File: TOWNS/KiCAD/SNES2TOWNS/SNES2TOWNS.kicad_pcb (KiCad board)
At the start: 2 copper layers, 13 parts, among them J1 DE9_Receptacle, J2 ArduinoP2_P7, J3 ArduinoP8_P13, J4 ArduinoA5_A0, J5 ArduinoVCC_GND, J6 SNES_CONTROLLER, J7 Conn_02x03_Odd_Even, U1 74LS157, U2 74LS157

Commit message: Change of plan.  PCB version will be for Arduino NANO.
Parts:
- removed J2: ArduinoP2_P7, Connector_PinHeader_2.54mm:PinHeader_1x06_P2.54mm_Vertical
- removed J3: ArduinoP8_P13, Connector_PinHeader_2.54mm:PinHeader_1x06_P2.54mm_Vertical
- removed J4: ArduinoA5_A0, Connector_PinHeader_2.54mm:PinHeader_1x06_P2.54mm_Vertical
- removed J5: ArduinoVCC_GND, Connector_PinHeader_2.54mm:PinHeader_1x06_P2.54mm_Vertical
- added J8: ArduinoNANOP1_P15, Connector_PinSocket_2.54mm:PinSocket_1x15_P2.54mm_Vertical, F.Cu at (116.8, 104.1)
- added J9: ArduinoNANOP16_P30, Connector_PinSocket_2.54mm:PinSocket_1x15_P2.54mm_Vertical, F.Cu at (101.6, 104.1)
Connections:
- R1 pad 1: GND -> /FJ6BTN
- R1 pad 2: /CPSF -> GND
- R2 pad 1: GND -> /CPSF
- R2 pad 2: /FJ6BTN -> GND
- U1 pad 16: +5V -> unconnected-(U1-VCC-Pad16)

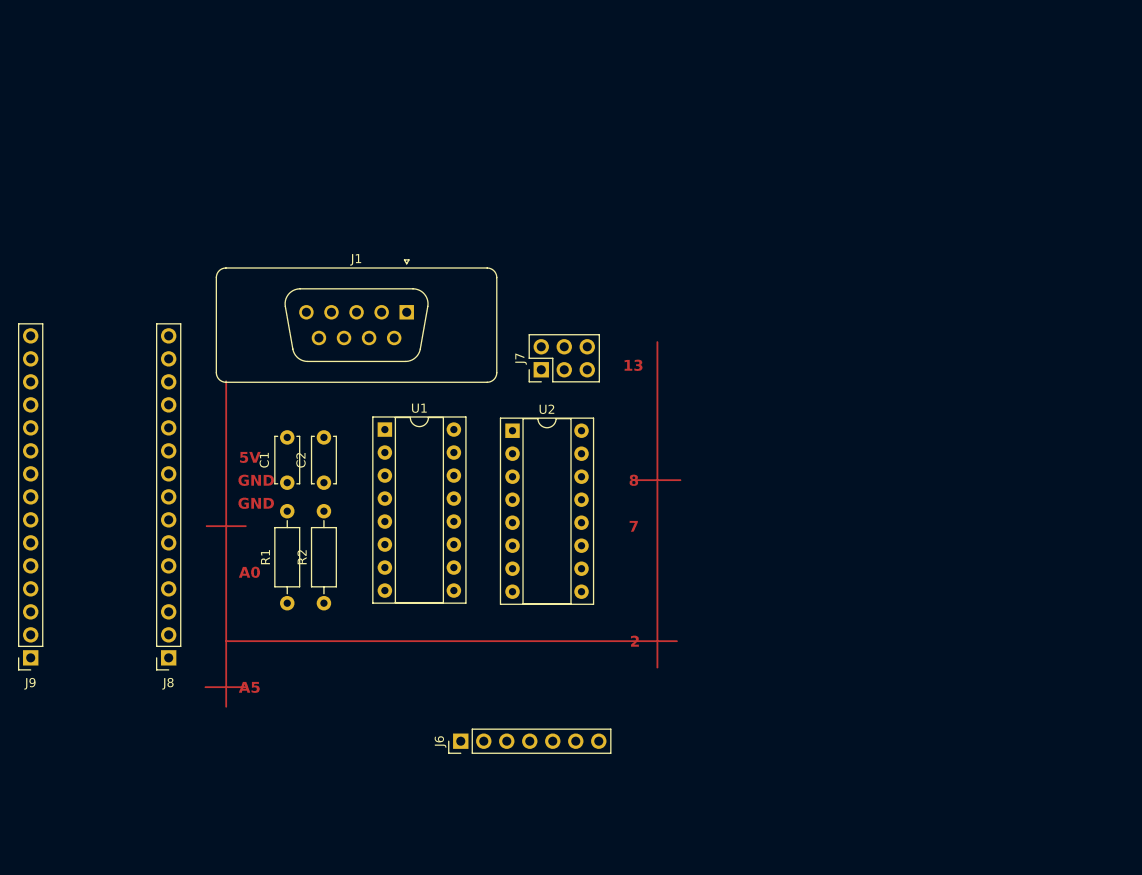
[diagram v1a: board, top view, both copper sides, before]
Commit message: PCB version will be for Arduino NANO.
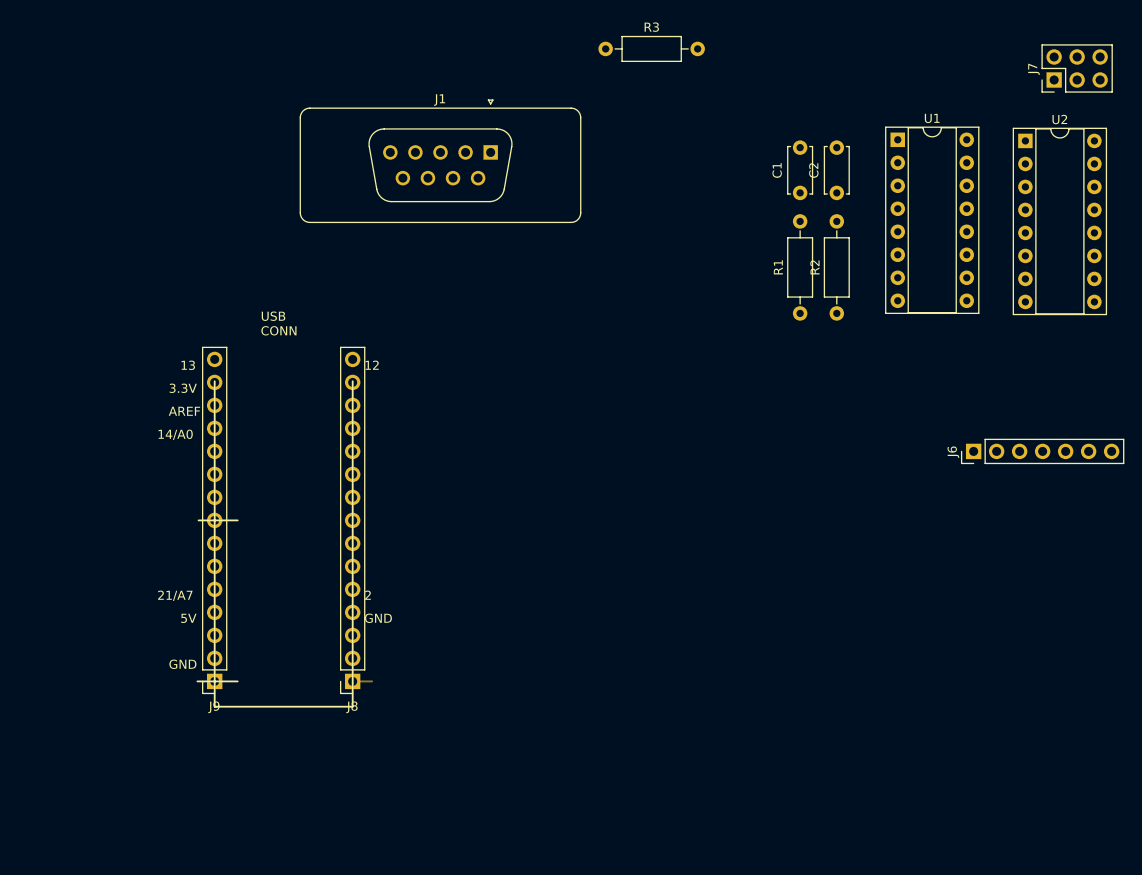
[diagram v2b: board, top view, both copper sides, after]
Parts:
- added R3: 220, Resistor_THT:R_Axial_DIN0207_L6.3mm_D2.5mm_P10.16mm_Horizontal, F.Cu at (165.1, 36.8)
- moved U2 65.1 mm to (211.5, 47.0)
- moved C1 65.1 mm to (186.6, 52.7)
- moved C2 65.1 mm to (190.6, 52.7)
- moved J6 65.1 mm to (205.7, 81.3)
- moved J7 65.1 mm to (214.6, 40.3)
- moved U1 65.1 mm to (197.4, 46.9)
- moved R1 65.1 mm to (186.6, 66.0)
- moved R2 65.1 mm to (190.6, 66.0)
- moved J9 20.5 mm to (121.9, 106.7)
- moved J8 20.5 mm to (137.2, 106.7)
- moved J1 19.9 mm to (152.4, 48.3)
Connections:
- J7 pad 3: +5V -> Net-(J7-Pin_3)
- J7 pad 4: +5V -> Net-(J7-Pin_3)
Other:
- board text added: "12"
- board text added: "14/A0"
- board text added: "21/A7"
- board text added: "3.3V"
- board text added: "AREF"
- board text added: "USB CONN"
- board text removed: "7"
- board text removed: "8"
- board text removed: "A0"
- board text removed: "A5"

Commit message: Changed registers and capacitors from THT to SMD.
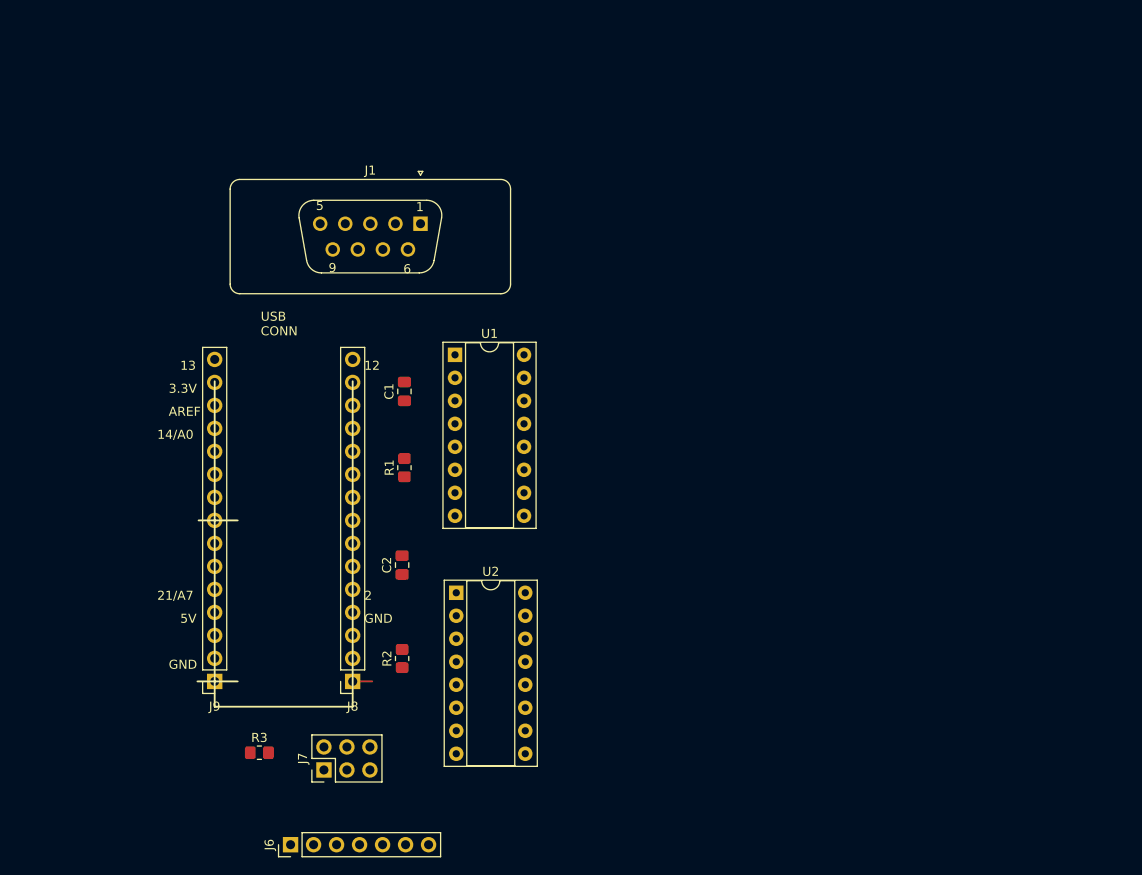
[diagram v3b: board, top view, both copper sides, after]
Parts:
- C1, C2: footprint Capacitor_THT:C_Disc_D5.0mm_W2.5mm_P5.00mm -> Capacitor_SMD:C_0805_2012Metric_Pad1.18x1.45mm_HandSolder
- R1, R2, R3: footprint Resistor_THT:R_Axial_DIN0207_L6.3mm_D2.5mm_P10.16mm_Horizontal -> Resistor_SMD:R_0805_2012Metric_Pad1.20x1.40mm_HandSolder
- moved J7 111.0 mm to (134.0, 116.5)
- moved J6 87.0 mm to (130.3, 124.7)
- moved R3 86.6 mm to (126.9, 114.6)
- moved U2 80.3 mm to (148.6, 96.9)
- moved C2 63.2 mm to (142.6, 93.8)
- moved R2 61.3 mm to (142.6, 104.2)
- moved U1 54.4 mm to (148.5, 70.6)
- moved C1 48.9 mm to (142.9, 74.7)
- moved R1 46.9 mm to (142.9, 83.1)
- moved J1 11.0 mm to (144.7, 56.1)
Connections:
- net /CPSF renamed /TWNS2BTN
- net /FJ6BTN renamed /TWNS6BTN
- net /L/A renamed /A/L
- net /START/B renamed /B/START
- J8 pad 10: unconnected-(J8-Pin_10-Pad10) -> /DOWN
- J8 pad 11: unconnected-(J8-Pin_11-Pad11) -> /LEFT
- J8 pad 12: unconnected-(J8-Pin_12-Pad12) -> /RIGHT
- J8 pad 13: unconnected-(J8-Pin_13-Pad13) -> /A
- J8 pad 14: unconnected-(J8-Pin_14-Pad14) -> /X
- J8 pad 15: unconnected-(J8-Pin_15-Pad15) -> /L
- J8 pad 5: unconnected-(J8-Pin_5-Pad5) -> /B
- J8 pad 6: unconnected-(J8-Pin_6-Pad6) -> /Y
- J8 pad 7: unconnected-(J8-Pin_7-Pad7) -> /SEL
- J8 pad 8: unconnected-(J8-Pin_8-Pad8) -> /START
- J8 pad 9: unconnected-(J8-Pin_9-Pad9) -> /UP
- J9 pad 15: unconnected-(J9-Pin_15-Pad15) -> /R
- U1 pad 13: /B -> /START
- U1 pad 14: /START -> /B
- U1 pad 16: unconnected-(U1-VCC-Pad16) -> +5V
- U1 pad 5: /L -> /A
- U1 pad 6: /A -> /L
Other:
- board text added: "1"
- board text added: "5"
- board text added: "6"
- board text added: "9"

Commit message: Design Change
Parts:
- J7: value Conn_02x03_Odd_Even -> Slide Switch
- moved J6 52.9 mm to (109.2, 76.2), turned to 0 degrees
- moved R3 38.7 mm to (162.8, 100.3)
- moved R1 38.1 mm to (110.5, 103.1)
- moved J7 30.2 mm to (162.6, 106.7)
- moved J1 29.8 mm to (166.4, 76.5), turned to 90 degrees
- moved R2 27.1 mm to (115.6, 103.1)
- moved U2 5.45 mm to (148.6, 91.4)
- moved U1 3.30 mm to (148.5, 67.3)
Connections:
- net /UP/R renamed /OUT_P1
- J1 pad 2: /DOWN/Y -> /OUT_P2
- J1 pad 3: /LEFT/X -> /OUT_P3
- J1 pad 4: /RIGHT/SEL -> /OUT_P4
- J1 pad 6: /A/L -> /OUT_P6
- J1 pad 7: /B/START -> /OUT_P7
- J8 pad 10: /DOWN -> /OUT_P4A
- J8 pad 11: /LEFT -> /OUT_P3B
- J8 pad 12: /RIGHT -> /OUT_P3A
- J8 pad 13: /A -> /OUT_P2B
- J8 pad 14: /X -> /OUT_P2A
- J8 pad 15: /L -> /OUT_P1B
- J8 pad 5: /B -> /OUT_P7B
- J8 pad 6: /Y -> /OUT_P7A
- J8 pad 7: /SEL -> /OUT_P6B
- J8 pad 8: /START -> /OUT_P6A
- J8 pad 9: /UP -> /OUT_P4B
- J9 pad 15: /R -> /OUT_P1A
- U1 pad 10: /Y -> /OUT_P3B
- U1 pad 11: /DOWN -> /OUT_P3A
- U1 pad 12: /B/START -> /OUT_P4
- U1 pad 13: /START -> /OUT_P4B
- U1 pad 14: /B -> /OUT_P4A
- U1 pad 2: /UP -> /OUT_P1A
- U1 pad 3: /R -> /OUT_P1B
- U1 pad 5: /A -> /OUT_P2A
- U1 pad 6: /L -> /OUT_P2B
- U1 pad 7: /A/L -> /OUT_P2
- U1 pad 9: /DOWN/Y -> /OUT_P3
- U2 pad 2: /LEFT -> /OUT_P6A
- U2 pad 3: /X -> /OUT_P6B
- U2 pad 4: /LEFT/X -> /OUT_P6
- U2 pad 5: /RIGHT -> /OUT_P7A
- U2 pad 6: /SEL -> /OUT_P7B
- U2 pad 7: /RIGHT/SEL -> /OUT_P7
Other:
- board text added: "SNES Game Controller to FM TOWNS Adapter Ver. 20230901 by CaptainYS http://www.ysflight.com"

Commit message: Making PCB
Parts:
- moved R1 5.33 mm to (115.8, 103.1), turned to -90 degrees
- moved R2 5.21 mm to (110.4, 103.1), turned to -90 degrees
- moved J7 2.04 mm to (162.4, 104.6)
- moved R3 1.59 mm to (163.9, 99.2), turned to 180 degrees
- turned C1 to -90 degrees
- turned C2 to -90 degrees
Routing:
- net GND: track 0.00 -> 192.0 mm
- net +5V: track 0.00 -> 137.9 mm
- net /TWNS2BTN: track 0.00 -> 107.9 mm
- net /TWNS6BTN: track 0.00 -> 105.4 mm
- net /COM: track 0.00 -> 81.4 mm
- net /OUT_P6: track 0.00 -> 61.0 mm
- net /OUT_P4A: track 0.00 -> 53.6 mm
- net /OUT_P7: track 0.00 -> 48.9 mm
- net /OUT_P4B: track 0.00 -> 39.5 mm
- net /OUT_P1: track 0.00 -> 36.6 mm
- net /OUT_P1A: track 0.00 -> 30.0 mm
- net /OUT_P3A: track 0.00 -> 20.5 mm
- net /OUT_P3B: track 0.00 -> 20.5 mm
- net /OUT_P2: track 0.00 -> 19.2 mm
- net /OUT_P7B: track 0.00 -> 14.6 mm
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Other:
- board text added: "CPSF"
- board text added: "TOWNS2BTN"
- board text added: "TOWNS6BTN"
